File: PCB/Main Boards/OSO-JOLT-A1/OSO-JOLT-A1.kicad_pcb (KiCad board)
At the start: 4 copper layers, 28.3 x 28.5 mm, 38 parts, among them J1 OSO_SWD, J2 FH19C-9S-0.5SH_10_, Q1 Q_NMOS_GSD, U1 ATSAML22J18A-MUT, U4 MIC5365-3.3YC5-TR, X1 Crystal

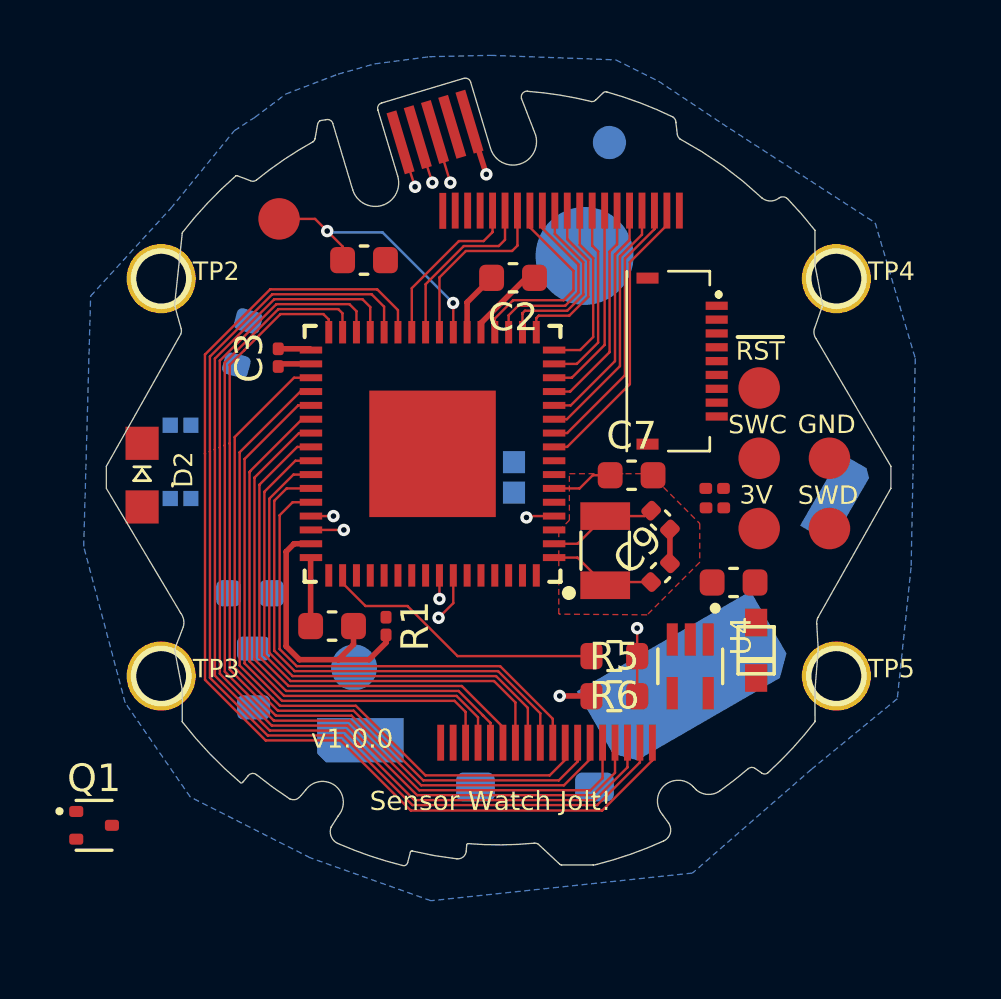
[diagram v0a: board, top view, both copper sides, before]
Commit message: Added all footprints
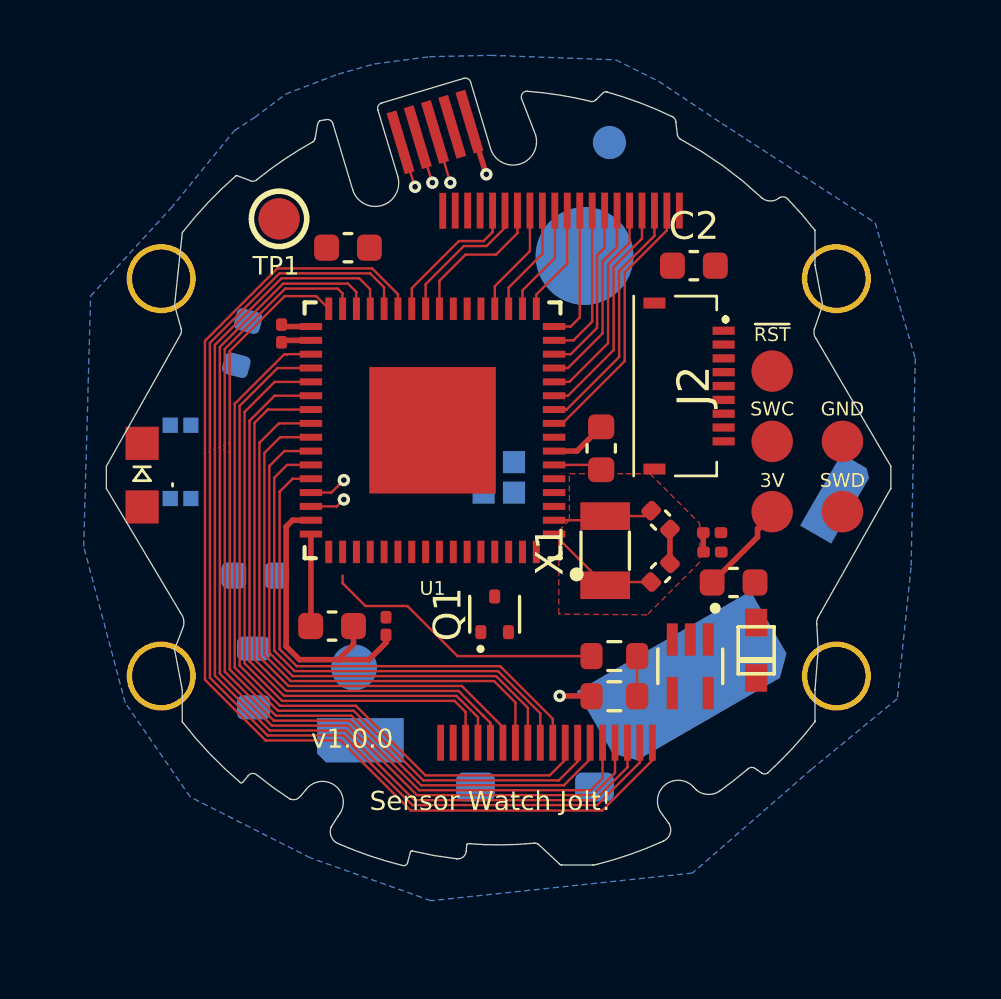
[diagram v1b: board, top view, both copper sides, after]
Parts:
- removed TP2, TP3, TP4, TP5: MICROBUILDER_TESTPOINTROUND1.5MM, OSO-SWAT-A1-05:MICROBUILDER_TESTPOINT_ROUND_1.5MM
- Q1: footprint Package_TO_SOT_SMD:SOT-523 -> OSO-SWAT-A1-05:SOT-523
- moved Q1 16.4 mm to (156.9, 107.5), turned to 90 degrees
- moved C2 6.55 mm to (164.1, 94.9), turned to 0 degrees
- moved R4 1.60 mm to (164.8, 105.2)
- moved R3 1.60 mm to (164.8, 104.5)
- moved C7 1.47 mm to (160.8, 101.5), turned to 90 degrees
- moved J2 0.93 mm to (162.7, 99.2)
- moved C3 0.88 mm to (149.2, 97.3)
- moved U1 0.85 mm to (154.7, 100.8)
- moved J1 0.77 mm to (168.2, 101.2)
- moved C6 0.73 mm to (151.6, 94.2)
- moved C1 0.67 mm to (148.2, 106.1), turned to 180 degrees
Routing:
- net /SWCLK_LIGHT: track 15.5 -> 0.00 mm, vias 1 -> 0
- net /SWDIO_MODE: track 12.0 -> 0.00 mm, vias 1 -> 0
- net /VLCD: track 9.89 -> 0.00 mm, vias 2 -> 0
- net /TEMPSENSE: track 10.7 -> 1.52 mm, vias 2 -> 0
- net /SEG7: track 7.30 -> 4.07 mm
- net /SEG6: track 6.97 -> 4.05 mm
- net /SEG5: track 6.63 -> 4.17 mm
- net /SEG4: track 6.13 -> 4.13 mm
- net /SEG19: track 19.5 -> 21.0 mm
- net /SEG3: track 6.38 -> 4.92 mm
- net /SEG18: track 19.9 -> 21.3 mm
- net /SEG17: track 20.4 -> 21.8 mm
- net /SEG16: track 25.5 -> 26.8 mm
- net /SEG8: track 6.65 -> 5.36 mm
- net VCC: track 7.80 -> 9.04 mm
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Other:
- board text removed: "3V"
- board text removed: "GND"
- board text removed: "SWC"
- board text removed: "SWD"
- board text removed: "~{RST}"

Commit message: All components placed in hopefully final location
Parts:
- moved R4 6.46 mm to (160.8, 100.2), turned to 90 degrees
- moved R3 4.92 mm to (160.8, 101.7), turned to -90 degrees
- moved C7 4.83 mm to (164.8, 104.1), turned to -90 degrees
- moved Q1 3.26 mm to (153.7, 108.0), turned to 180 degrees
- moved R1 2.06 mm to (151.8, 109.7), turned to 180 degrees
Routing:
- net /BUZZER: track 0.00 -> 2.62 mm
- net +3V3: track 1.77 -> 0.00 mm
- net /SEG20: track 20.3 -> 21.4 mm
- net /SEG19: track 21.0 -> 21.9 mm
- net /SEG18: track 21.3 -> 22.1 mm
- net VCC: track 9.04 -> 8.33 mm
- net GND: track 17.5 -> 16.8 mm
- net /SEG17: track 21.8 -> 22.3 mm
- net /SEG23: track 18.8 -> 19.4 mm

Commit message: Finished first pass at routing
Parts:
- moved R4 1.60 mm to (160.8, 101.8), turned to -90 degrees
- moved R3 1.50 mm to (160.8, 100.2), turned to 90 degrees
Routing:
- net /~{RESET}: track 0.00 -> 30.3 mm, vias 0 -> 2
- net /SWDIO_MODE: track 0.00 -> 30.0 mm, vias 0 -> 2
- net VCC: track 8.33 -> 37.0 mm, vias 1 -> 10
- net GND: track 16.8 -> 44.3 mm, vias 1 -> 12
- net /SWCLK_LIGHT: track 0.00 -> 25.7 mm, vias 0 -> 2
- net VBUS: track 1.69 -> 24.5 mm, vias 1 -> 2
- net /ADJUST: track 0.00 -> 18.9 mm, vias 0 -> 1
- net +3V3: track 0.00 -> 18.5 mm
- net /START: track 0.00 -> 17.0 mm, vias 0 -> 1
- net /SCL: track 0.00 -> 15.9 mm, vias 0 -> 2
- net /SDA: track 0.00 -> 15.5 mm, vias 0 -> 2
- net /A3/D0/CS: track 0.00 -> 13.7 mm, vias 0 -> 2
- net /TEMPSENSE: track 1.52 -> 14.5 mm, vias 0 -> 2
- net /A1_SCK: track 0.00 -> 12.4 mm, vias 0 -> 2
- net /A4/D1/MISO: track 0.00 -> 12.0 mm, vias 0 -> 2
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
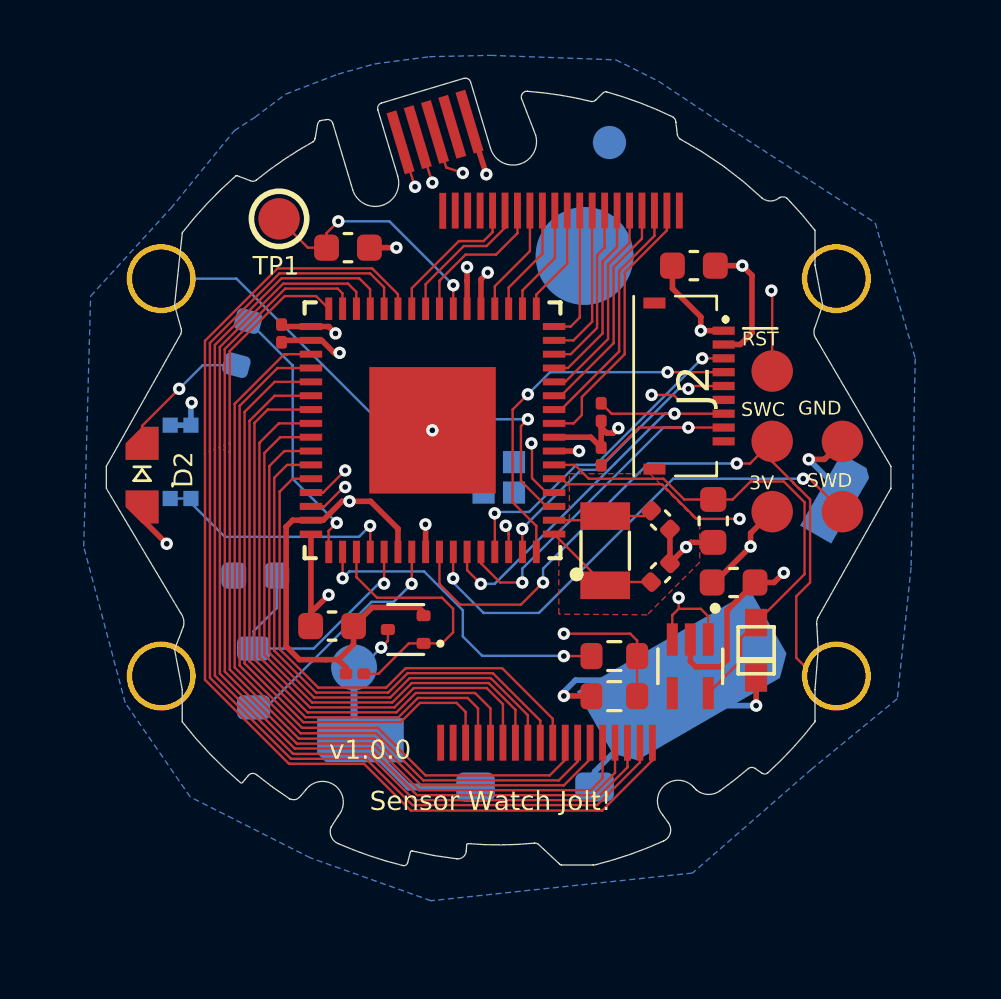
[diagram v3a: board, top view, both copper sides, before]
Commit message: Made board 2 layer for 0.4mm thickness
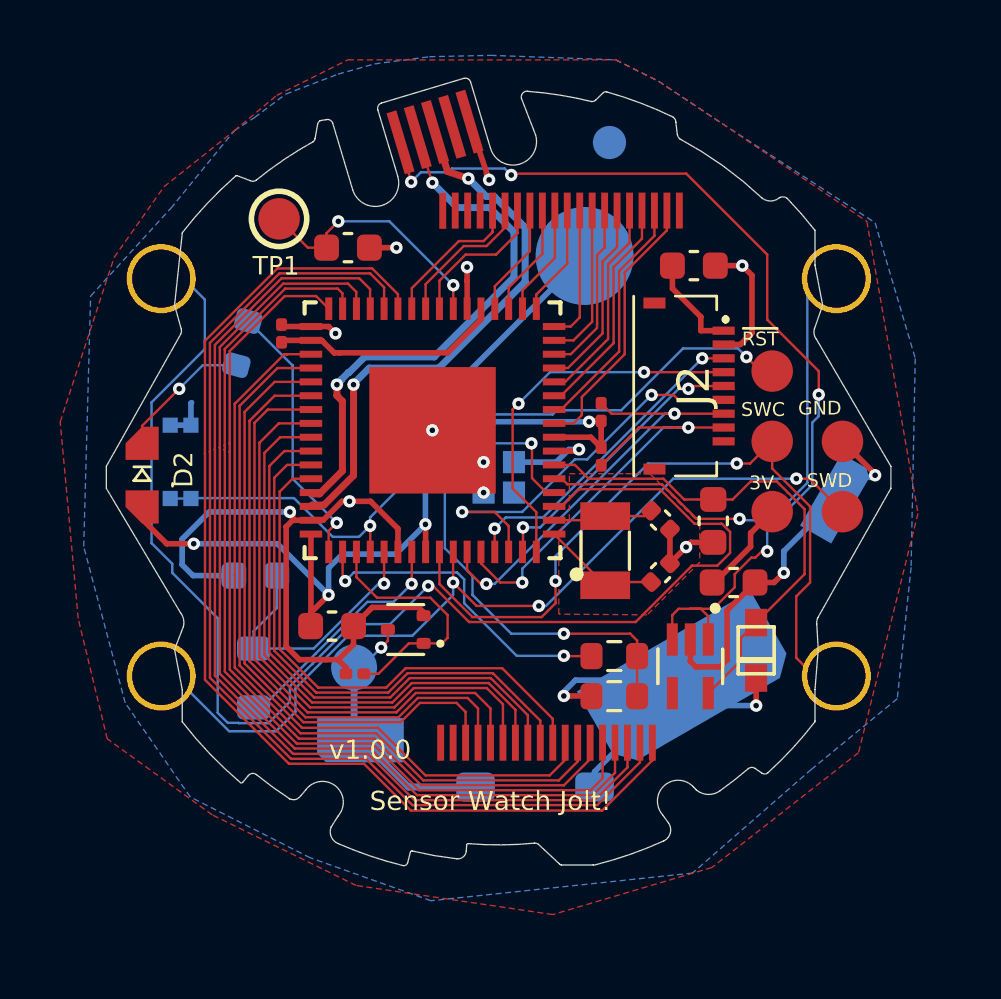
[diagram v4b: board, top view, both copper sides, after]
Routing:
- net /ADJUST: track 18.9 -> 48.6 mm
- net VCC: track 37.0 -> 61.5 mm, vias 10 -> 6
- net GND: track 44.3 -> 67.3 mm, vias 12 -> 14
- net VBUS: track 24.5 -> 35.3 mm, vias 2 -> 4
- net /TEMPSENSE: track 14.5 -> 19.6 mm
- net /USB_N: track 15.0 -> 19.8 mm
- net /~{RESET}: track 30.3 -> 26.6 mm
- net /USB_P: track 16.7 -> 20.1 mm
- net /SWDIO_MODE: track 30.0 -> 31.9 mm, vias 2 -> 3
- net /A1_SCK: track 12.4 -> 14.1 mm
- net /SWCLK_LIGHT: track 25.7 -> 26.7 mm
- net /START: track 17.0 -> 17.7 mm
- added copper zone on F.Cu, net VCC
- removed copper zone on In2.Cu, net GND
- removed copper zone on In1.Cu, net VCC
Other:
- copper layers 4 -> 2

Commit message: Made back components larger in case I want to hand-solder them
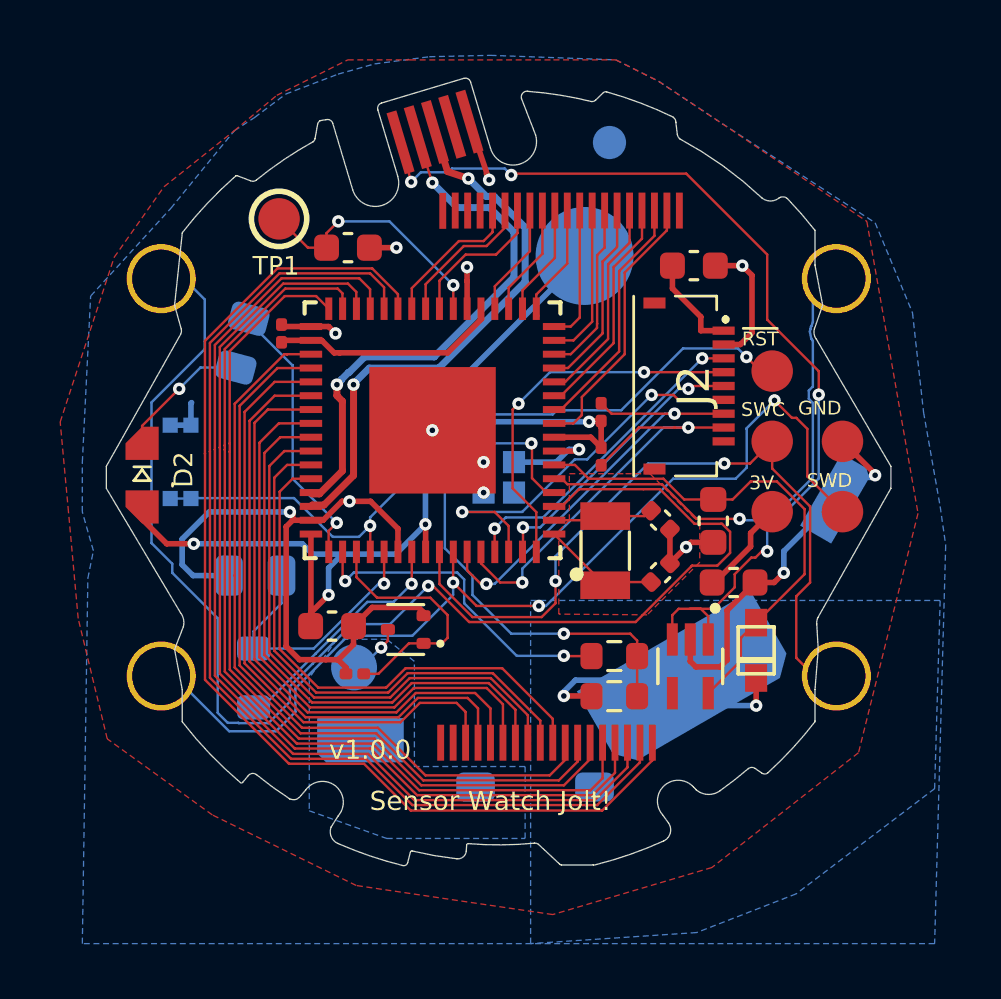
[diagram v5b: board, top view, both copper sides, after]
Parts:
- C1: footprint Capacitor_SMD:C_0603_1608Metric -> Capacitor_SMD:C_0805_2012Metric
- R2: footprint Resistor_SMD:R_0603_1608Metric -> Resistor_SMD:R_0805_2012Metric
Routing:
- net /BUZZER_HV: track 9.61 -> 2.08 mm
- net VCC: track 61.5 -> 56.2 mm
- net /SWDIO_MODE: track 31.9 -> 36.1 mm
- added copper zone on B.Cu, net /BUZZER_HV
- added copper zone on B.Cu, net VCC

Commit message: Added Gerber files
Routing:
- net /SDA: track 15.5 -> 16.4 mm
